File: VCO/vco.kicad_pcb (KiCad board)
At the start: 2 copper layers, 50 x 100 mm, 103 parts, among them J1 Audio-Jack-2, J10 Audio-Jack-2, J11 Conn_02x08_Top_Bottom, J2 Audio-Jack-2, J3 Audio-Jack-2, J4 Audio-Jack-2, J5 Audio-Jack-2, J6 Audio-Jack-2, J7 Audio-Jack-2, J8 Audio-Jack-2, J9 Audio-Jack-2, Q1 Q_NJFET_DSG, U1 LM13700, U2 TL072, U3 OP275, U4 TL074, U5 SSM2210, U6 TL072, U7 TL071

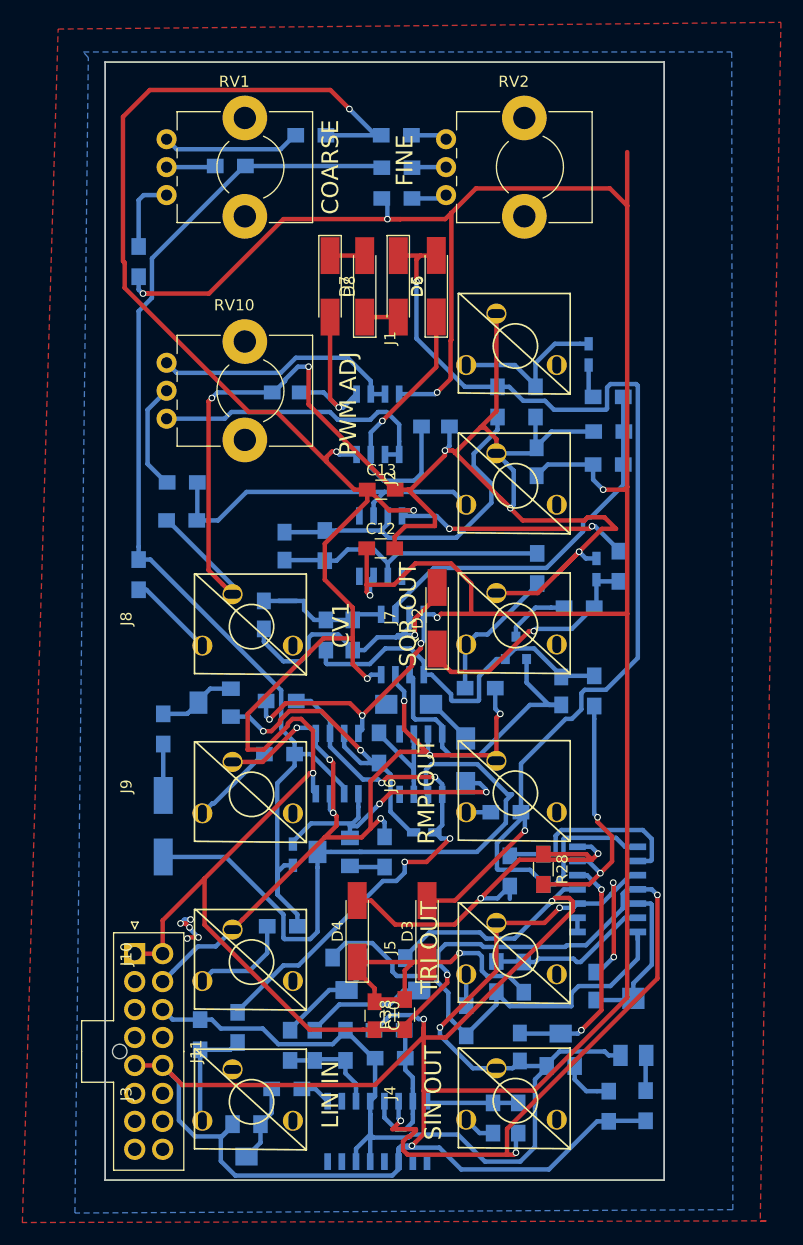
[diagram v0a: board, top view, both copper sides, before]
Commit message: Changed Pot
Trimmer potentiometer was too expensive, updated pcb and gerbers for cheaper trimmer pot
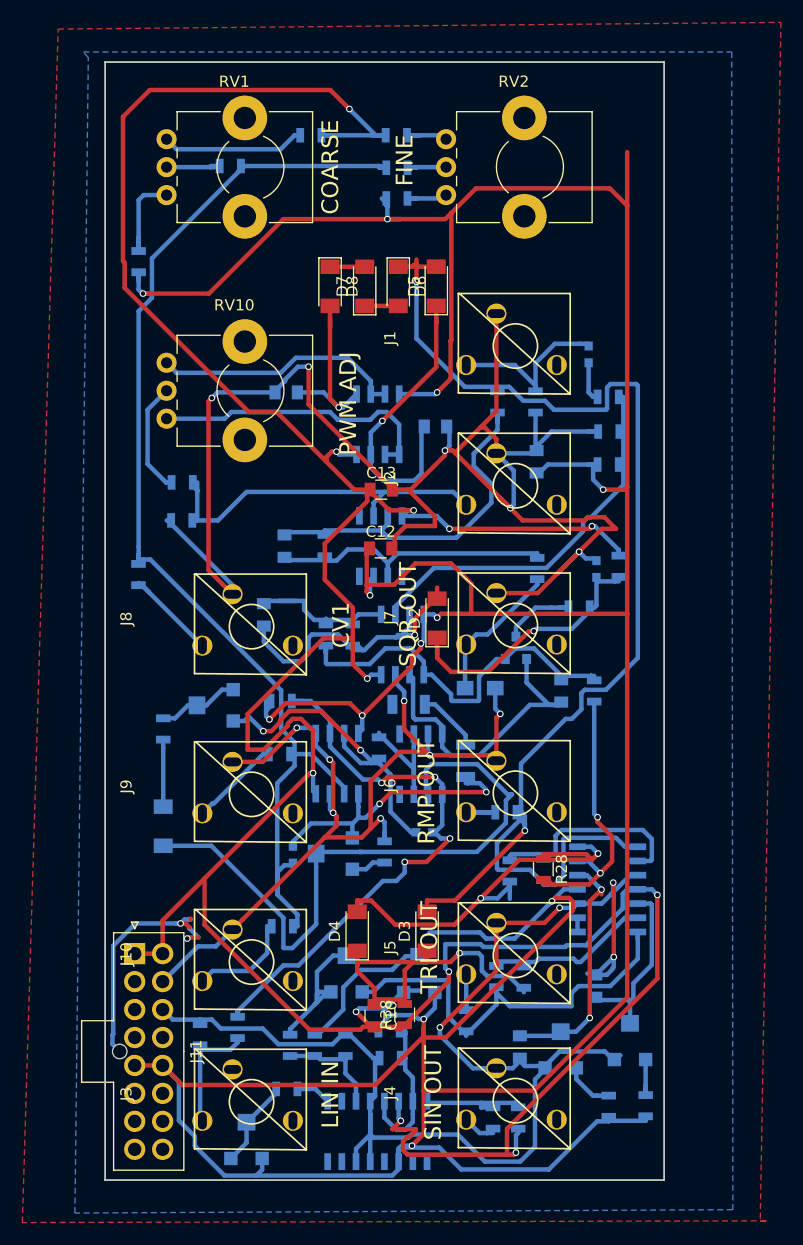
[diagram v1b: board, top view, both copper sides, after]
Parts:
- removed G***: LOGO, OPENHARDWARE:OSHWLOGO0.3IN
- C1, C3, C7, C8: footprint Capacitors_SMD:C_0603_HandSoldering -> Capacitors_SMD:C_0603
- C10, C11, C12, C13, C14, C15, C2, C4, C5, C6, C9: footprint Capacitors_SMD:C_0805_HandSoldering -> Capacitors_SMD:C_0805
- D1, D2, D3, D4, D5, D6, D7, D8: footprint Diodes_SMD:D_MiniMELF_Handsoldering -> Diodes_SMD:D_MiniMELF
- R1, R10, R11, R12, R13, R14, R15, R16, R17, R18, R19, R2, R20, R21, R22, R23, R24, R25, R26, R27, R28, R29, R3, R30, R31, R32, R33, R34, R35, R36, R37, R38, R39, R4, R40, R41, R42, R43, R44, R45, R46, R47, R48, R5, R6, R7, R9: footprint Resistors_SMD:R_0805_HandSoldering -> Resistors_SMD:R_0805
- RV3, RV4, RV5, RV6, RV7, RV9: footprint Potentiometers:Potentiometer_Trimmer_Bourns_3214W -> Potentiometers:Potentiometer_Trimmer-EVM3E
- RV8: footprint Potentiometers:Potentiometer_Trimmer_Bourns_3214X -> Potentiometers:Potentiometer_Trimmer-EVM3E
- TH1, TH2: footprint Resistors_SMD:R_1206_HandSoldering -> Resistors_SMD:R_1206
- moved RV8 1.33 mm to (196.9, 117.6), turned to 180 degrees
- moved RV5 0.24 mm to (159.8, 87.5), turned to 270 degrees
- moved RV3 0.16 mm to (170.5, 100.8), turned to 270 degrees
- turned RV4 to 180 degrees
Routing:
- net (no net): track 4.56 -> 21.2 mm, vias 5 -> 2
- net -12V: track 287.0 -> 299.8 mm, vias 11 -> 12
- net GND: track 339.9 -> 347.3 mm
- net Net-(R32-Pad1): track 10.0 -> 13.8 mm
- net SINSHAPER: track 41.7 -> 37.9 mm
- net Net-(C1-Pad1): track 101.9 -> 105.7 mm
- net Net-(D3-Pad2): track 116.7 -> 120.2 mm
- net Net-(C10-Pad1): track 28.5 -> 31.4 mm
- net RMP: track 2.85 -> 5.45 mm
- net Net-(R27-Pad1): track 11.0 -> 13.4 mm
- net Net-(D4-Pad2): track 36.5 -> 38.8 mm
- net Net-(C9-Pad1): track 13.8 -> 16.0 mm
- net Net-(C8-Pad1): track 22.4 -> 24.4 mm
- net Net-(R41-Pad2): track 8.22 -> 10.2 mm
- net Net-(C15-Pad2): track 15.2 -> 17.1 mm
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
